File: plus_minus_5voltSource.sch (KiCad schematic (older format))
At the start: 8 parts, among them P1 CONN_01X03, U1 7660

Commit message: redesigned to have indicator leds, and voltage regulators
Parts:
- added SW?: SW_Push, symbol SW_Push
- added U?: LM79L05_TO92, TO_SOT_Packages_THT:TO-92_Inline_Narrow_Oval, symbol LM79L05_TO92
- added U?: LM7805_TO220, TO_SOT_Packages_THT:TO-220_Vertical, symbol LM7805_TO220
- D1, D2: symbol LED -> LED-RESCUE-plus_minus_5voltSource
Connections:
- net GND: now also U?.1 (GND), U?.2 (GND)
- net V-: now also U?.2 (VI); no longer P1.1 (P1)
- net VCC: now also SW?.1, U?.1 (VI); no longer P1.3 (P3), R1.1, U1.8 (Vin)
- new net: R1.1, SW?.2
- new net Vnreg: P1.1 (P1), U?.3 (VO)
- new net Vpreg: P1.3 (P3), U1.8 (Vin), U?.3 (VO)
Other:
- moved on the sheet: C1, C2, D1, D2, R1, R2, U1

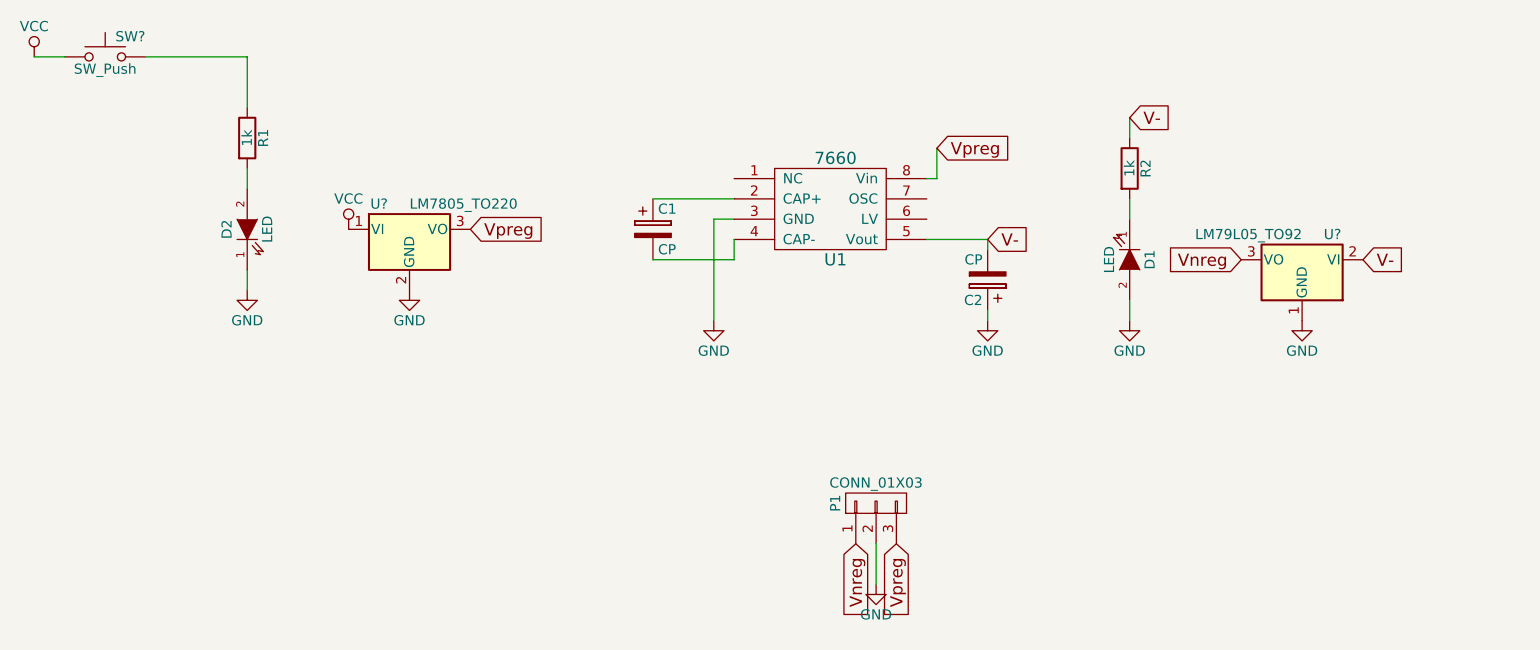
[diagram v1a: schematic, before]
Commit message: added capacitors to voltage regulator lines.
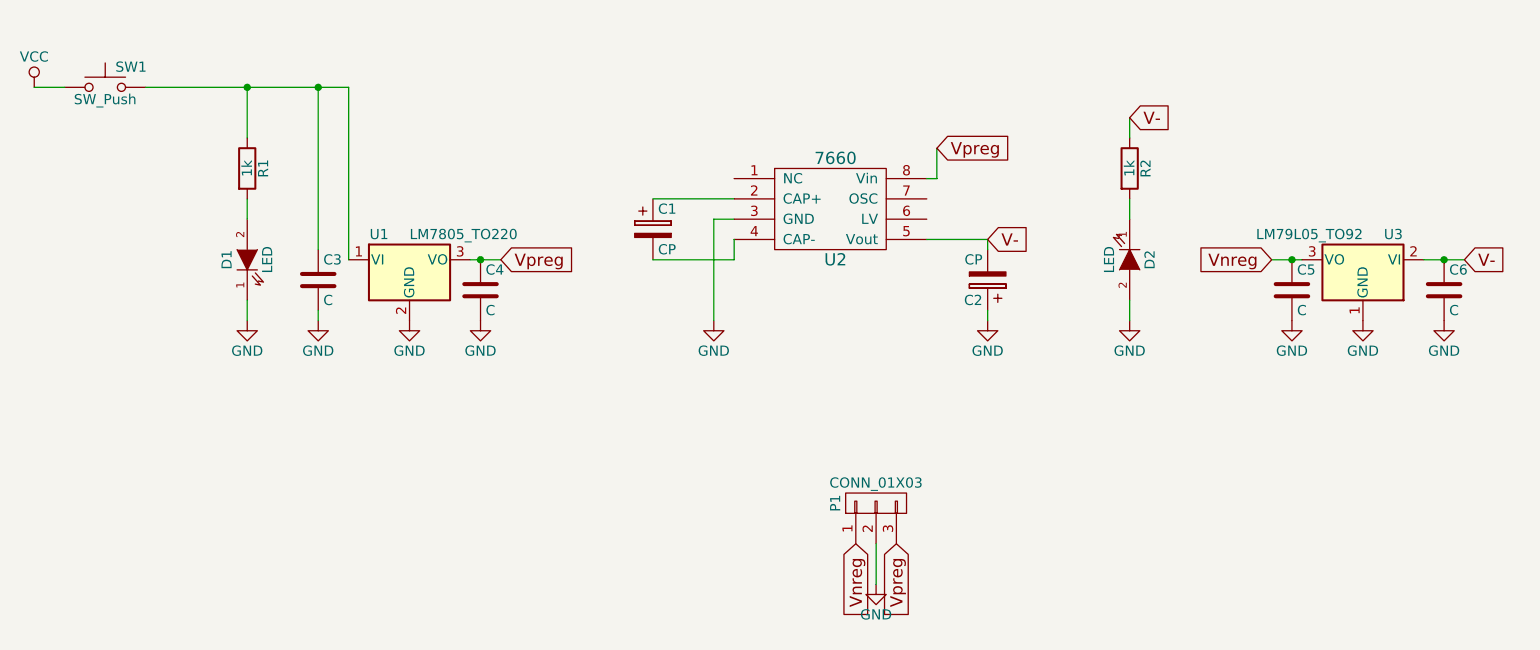
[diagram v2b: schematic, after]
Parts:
- added C3, C4, C5, C6: C, symbol C
- gave numbers to parts that had none: 3
- renumbered D2 to D1, D1 to D2, U1 to U2
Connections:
- net GND: now also C3.2, C4.2, C5.2, C6.2
- net V-: now also C6.1
- net VCC: no longer U1.1 (VI)
- net Vnreg: now also C5.1
- net Vpreg: now also C4.1
- net at R1.1, SW1.2: now also U1.1 (VI), C3.1
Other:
- moved on the sheet: D1, R1, SW1, U1, U3
